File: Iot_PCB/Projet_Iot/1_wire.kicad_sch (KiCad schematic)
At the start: 9 parts

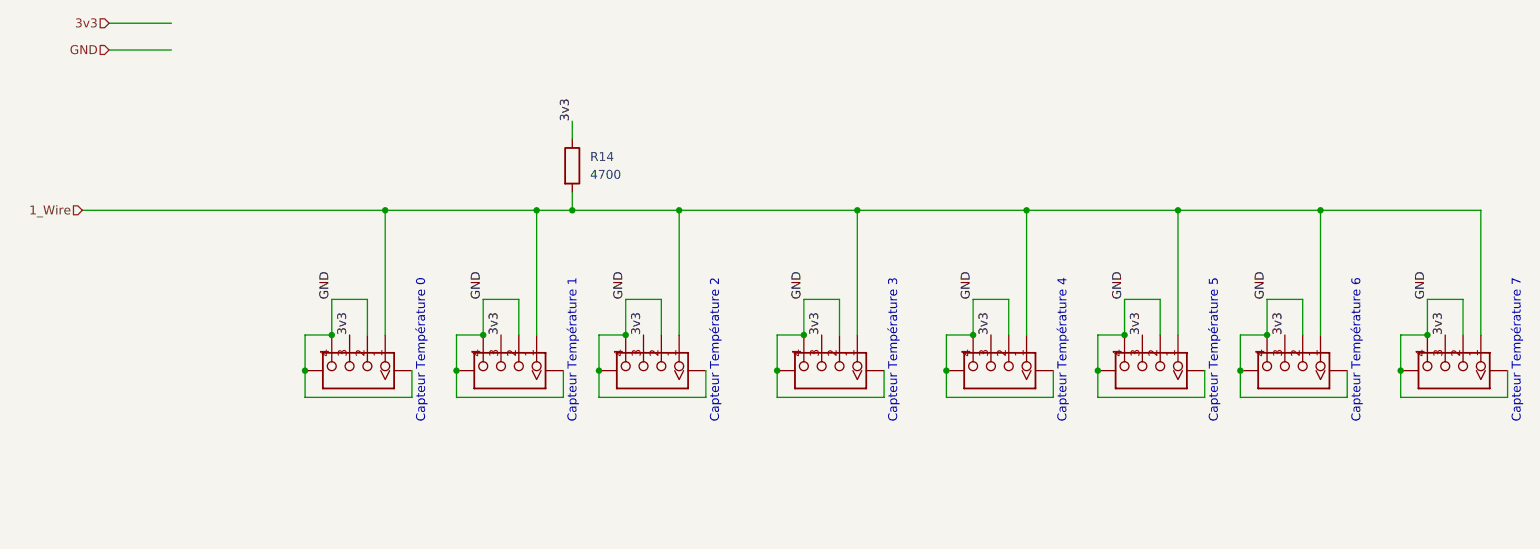
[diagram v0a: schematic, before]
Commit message: remplacement des grove lora par des vrais
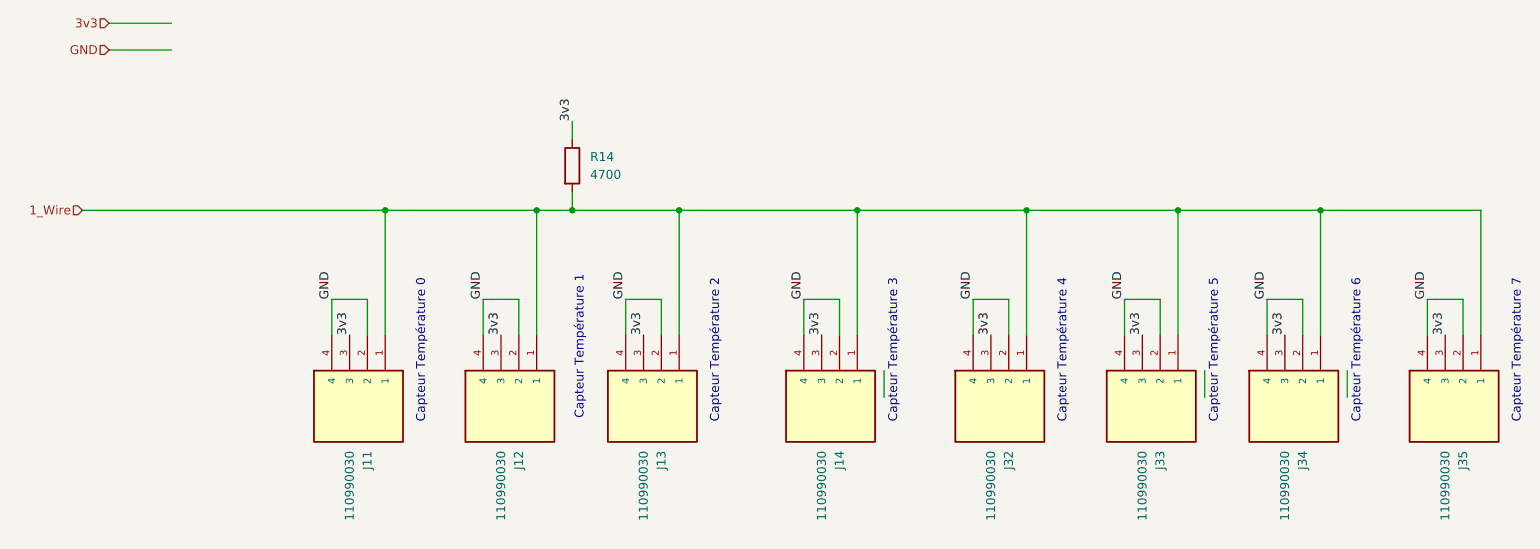
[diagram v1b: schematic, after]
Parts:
- removed J24, J25, J26, J27, J28, J29, J30, J31: ~, Lora:HW4-SMD-2.0, symbol Lora-eagle-import:GROVE-CONNECTOR-SMD'DD'
- added J11, J12, J13, J14, J32, J33, J34, J35: 110990030, 110990030:SEEED_110990030, symbol grove:110990030
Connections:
- net 1_Wire: now also J11.1, J12.1, J13.1, J14.1, J32.1, J33.1, J34.1, J35.1
- net 3v3: now also J11.3, J12.3, J13.3, J14.3, J32.3, J33.3, J34.3, J35.3
- net GND: now also J11.2, J11.4, J12.2, J12.4, J13.2, J13.4, J14.2, J14.4, J32.2, J32.4, J33.2, J33.4, J34.2, J34.4, J35.2, J35.4

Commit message: update 1-wire, pull_up i2c, switch load added but not configured yet (wait for test)
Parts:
- removed J32, J33, J34, J35: 110990030, 110990030:SEEED_110990030, symbol grove:110990030
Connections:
- net 1_Wire: now also J11.2, J12.2, J13.2, J14.2
- net GND: no longer J11.2, J12.2, J13.2, J14.2
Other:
- note added: "Capteur Température 0/1"
- note added: "Capteur Température 2/3"
- note added: "Capteur Température 4/5"
- note added: "Capteur Température 6/7"
- note removed: "Capteur Température 0"
- note removed: "Capteur Température 1"
- note removed: "Capteur Température 2"
- note removed: "Capteur Température 3"
- note removed: "Capteur Température 4"
- note removed: "Capteur Température 5"
- note removed: "Capteur Température 6"
- note removed: "Capteur Température 7"

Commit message: build(kicad): add a trace to every schematic
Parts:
- R14: footprint (none) -> Resistor_THT:R_Axial_DIN0207_L6.3mm_D2.5mm_P10.16mm_Horizontal
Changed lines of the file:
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@@
 (kicad_sch
-	(version 20231120)
+	(version 20250114)
 	(generator "eeschema")
-	(generator_version "8.0")
+	(generator_version "9.0")
 	(paper "A4")
+	(text "Capteur Température 2/3"
+		(exclude_from_sim no)
+		(at 116.586 105.918 90)
+		(effects
+			(font
+				(size 1.27 1.27)
+			)
+		)
+	)
+	(text "Capteur Température 4/5"
+		(exclude_from_sim no)
+		(at 135.89 106.426 90)
+		(effects
+			(font
+				(size 1.27 1.27)
+			)
+		)
+	)
+	(text "Capteur Température 6/7"
+		(exclude_from_sim no)
+		(at 161.29 106.426 90)
+		(effects
+			(font
+				(size 1.27 1.27)
+			)
+		)
+	)
+	(text "Capteur Température 0/1\n"
+		(exclude_from_sim no)
+		(at 93.98 106.426 90)
+		(effects
+			(font
+				(size 1.27 1.27)
+			)
+		)
+	)
 	(junction
 		(at 110.49 86.36)
@@
 		)
 	)
-	(text "Capteur Température 2/3"
-		(exclude_from_sim no)
-		(at 116.586 105.918 90)
-		(effects
-			(font
-				(size 1.27 1.27)
-			)
-		)
-	)
-	(text "Capteur Température 4/5"
-		(exclude_from_sim no)
-		(at 135.89 106.426 90)
-		(effects
-			(font
-				(size 1.27 1.27)
-			)
-		)
-	)
-	(text "Capteur Température 6/7"
-		(exclude_from_sim no)
-		(at 161.29 106.426 90)
-		(effects
-			(font
-				(size 1.27 1.27)
-			)
-		)
-	)
-	(text "Capteur Température 0/1\n"
-		(exclude_from_sim no)
-		(at 93.98 106.426 90)
-		(effects
-			(font
-				(size 1.27 1.27)
-			)
-		)
-	)
 	(label "3v3"
 		(at 125.73 104.14 90)
-		(fields_autoplaced yes)
 		(effects
 			(font
@@
 	(label "3v3"
 		(at 83.82 104.14 90)
-		(fields_autoplaced yes)
 		(effects
 			(font
@@
 	(label "GND"
 		(at 148.59 99.06 90)
-		(fields_autoplaced yes)
 		(effects
 			(font
@@
 	(label "GND"
 		(at 81.28 99.06 90)
-		(fields_autoplaced yes)
 		(effects
 			(font
@@
 	(label "3v3"
 		(at 105.41 104.14 90)
-		(fields_autoplaced yes)
 		(effects
 			(font
@@
 	(label "3v3"
 		(at 115.57 73.66 90)
-		(fields_autoplaced yes)
 		(effects
 			(font
@@
 	(label "GND"
 		(at 102.87 99.06 90)
-		(fields_autoplaced yes)
 		(effects
 			(font
@@
 	(label "GND"
 		(at 123.19 99.06 90)
-		(fields_autoplaced yes)
 		(effects
 			(font
@@
 	(label "3v3"
 		(at 151.13 104.14 90)
-		(fields_autoplaced yes)
 		(effects
 			(font
@@
 		(shape input)
 		(at 45.72 86.36 180)
-		(fields_autoplaced yes)
 		(effects
 			(font
@@
 		(shape input)
 		(at 49.53 59.69 180)
-		(fields_autoplaced yes)
 		(effects
 			(font
@@
 		(shape input)
 		(at 49.53 63.5 180)
-		(fields_autoplaced yes)
 		(effects
 			(font
@@
 			)
 		)
-		(property "Footprint" ""
+		(property "Footprint" "Resistor_THT:R_Axial_DIN0207_L6.3mm_D2.5mm_P10.16mm_Horizontal"
 			(at 113.792 80.01 90)
 			(effects

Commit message: build(kicad) : start PCB
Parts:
- J11, J12, J13, J14: footprint 110990030:SEEED_110990030 -> Grove:SEEED_110990030
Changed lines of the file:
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@@
 			)
 		)
-		(property "Footprint" "110990030:SEEED_110990030"
+		(property "Footprint" "Grove:SEEED_110990030"
 			(at 86.36 114.3 0)
 			(effects
@@
 			)
 		)
-		(property "Footprint" "110990030:SEEED_110990030"
+		(property "Footprint" "Grove:SEEED_110990030"
 			(at 107.95 114.3 0)
 			(effects
@@
 			)
 		)
-		(property "Footprint" "110990030:SEEED_110990030"
+		(property "Footprint" "Grove:SEEED_110990030"
 			(at 128.27 114.3 0)
 			(effects
@@
 			)
 		)
-		(property "Footprint" "110990030:SEEED_110990030"
+		(property "Footprint" "Grove:SEEED_110990030"
 			(at 153.67 114.3 0)
 			(effects
